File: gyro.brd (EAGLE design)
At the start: 27.9 x 15.2 mm, 12 parts, among them IC3 FXAS21002C

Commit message: gyro gotowe! w lbr pozmieniane poligony
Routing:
- net GND: track 6.35 -> 2.59 mm, vias 14 -> 15
- net MOSI: track 23.6 -> 25.7 mm
- net VDDIO: track 4.77 -> 6.41 mm
- net MISO: track 26.9 -> 27.8 mm

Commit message: gerbery do gyro
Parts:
- renumbered SV1 to SPI, SV2 to ZAS
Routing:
- net GND: vias 15 -> 14
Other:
- board text added: "CLK"
- board text added: "CSA"
- board text added: "CSG"
- board text added: "GND"
- board text added: "INTA"
- board text added: "K. Trzcinski K. Dworakowski 2015"
- board text added: "MISO"
- board text added: "MOSI"
- board text added: "VCC"
- board text added: "X"
- board text added: "Y"

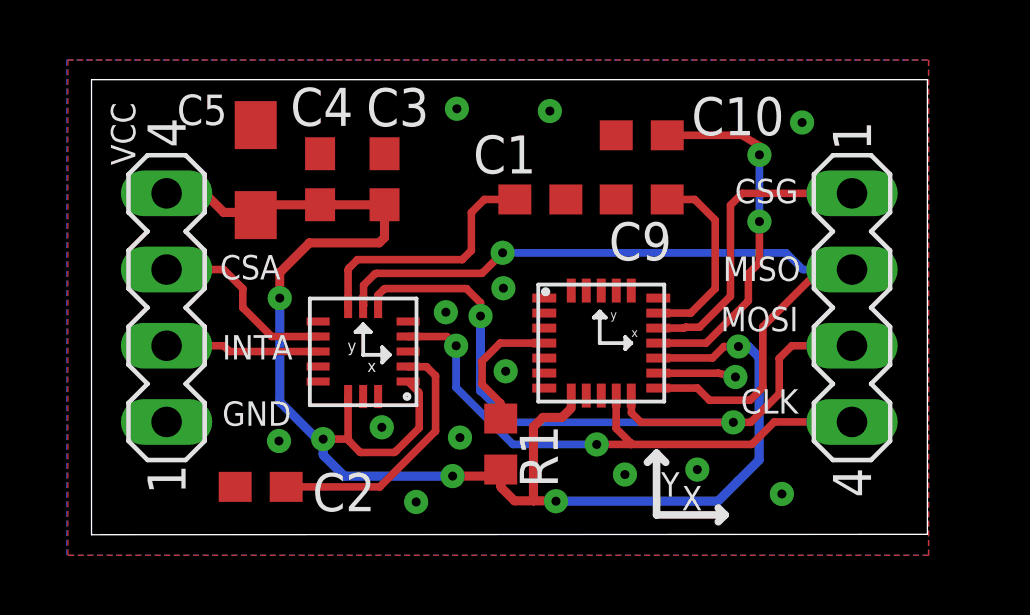
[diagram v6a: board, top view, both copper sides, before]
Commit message: wszystko polaczone, zmiana w gyro z vcc na +3v3
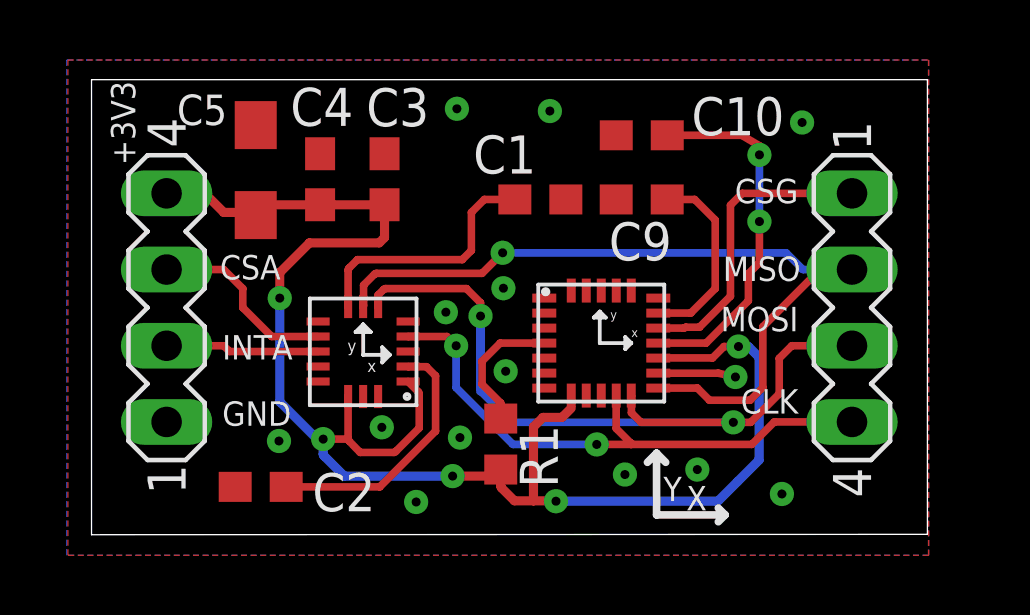
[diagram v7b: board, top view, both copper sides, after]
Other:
- board text added: "+3V3"
- board text removed: "VCC"
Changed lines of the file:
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@@
 <grid distance="3" unitdist="mil" unit="mil" style="lines" multiple="1" display="yes" altdistance="0.5" altunitdist="mil" altunit="mil"/>
 <layers>
-<layer number="1" name="Top" color="4" fill="1" visible="yes" active="yes"/>
+<layer number="1" name="Top" color="4" fill="1" visible="no" active="yes"/>
 <layer number="2" name="Route2" color="1" fill="3" visible="no" active="no"/>
 <layer number="3" name="Route3" color="4" fill="3" visible="no" active="no"/>
@@
 <layer number="14" name="Route14" color="1" fill="6" visible="no" active="no"/>
 <layer number="15" name="Route15" color="4" fill="6" visible="no" active="no"/>
-<layer number="16" name="Bottom" color="1" fill="1" visible="yes" active="yes"/>
+<layer number="16" name="Bottom" color="1" fill="1" visible="no" active="yes"/>
 <layer number="17" name="Pads" color="2" fill="1" visible="yes" active="yes"/>
 <layer number="18" name="Vias" color="2" fill="1" visible="yes" active="yes"/>
 <layer number="19" name="Unrouted" color="6" fill="1" visible="no" active="yes"/>
 <layer number="20" name="Dimension" color="15" fill="1" visible="no" active="yes"/>
-<layer number="21" name="tPlace" color="7" fill="1" visible="yes" active="yes"/>
+<layer number="21" name="tPlace" color="7" fill="1" visible="no" active="yes"/>
 <layer number="22" name="bPlace" color="7" fill="1" visible="yes" active="yes"/>
-<layer number="23" name="tOrigins" color="15" fill="1" visible="yes" active="yes"/>
+<layer number="23" name="tOrigins" color="15" fill="1" visible="no" active="yes"/>
 <layer number="24" name="bOrigins" color="15" fill="1" visible="no" active="yes"/>
-<layer number="25" name="tNames" color="7" fill="1" visible="yes" active="yes"/>
+<layer number="25" name="tNames" color="7" fill="1" visible="no" active="yes"/>
 <layer number="26" name="bNames" color="7" fill="1" visible="yes" active="yes"/>
 <layer number="27" name="tValues" color="7" fill="1" visible="no" active="yes"/>
@@
 <layer number="101" name="Patch_Top" color="12" fill="4" visible="no" active="yes"/>
 <layer number="102" name="Vscore" color="7" fill="1" visible="no" active="yes"/>
-<layer number="103" name="tMap" color="7" fill="1" visible="yes" active="yes"/>
+<layer number="103" name="tMap" color="7" fill="1" visible="no" active="yes"/>
 <layer number="104" name="Name" color="16" fill="1" visible="no" active="yes"/>
 <layer number="105" name="tPlate" color="7" fill="1" visible="no" active="yes"/>
@@
 <text x="26.1366" y="91.8972" size="0.8128" layer="25" rot="R180">CLK</text>
 <text x="6.9342" y="90.678" size="0.8128" layer="25">GND</text>
-<text x="4.0386" y="99.3648" size="0.8128" layer="25" rot="R90">VCC</text>
+<text x="4.0386" y="99.3648" size="0.8128" layer="25" rot="R90">+3V3</text>
 <text x="24.2316" y="94.4118" size="1.4224" layer="26" font="vector" ratio="12" distance="41" rot="MR0">K. Trzcinski
 K. Dworakowski
@@
 <wire x1="23.6982" y1="87.7062" x2="23.4696" y2="87.9348" width="0.254" layer="21"/>
 <wire x1="23.6982" y1="87.7062" x2="23.4696" y2="87.4776" width="0.254" layer="21"/>
-<text x="21.5646" y="88.3158" size="0.8128" layer="21">Y</text>
-<text x="22.2504" y="87.8586" size="0.8128" layer="21">X</text>
+<text x="21.6408" y="88.1634" size="0.8128" layer="21">Y</text>
+<text x="22.4028" y="87.8586" size="0.8128" layer="21">X</text>
 </plain>
 <attributes>

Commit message: poprawa bledow, dodanie rezystorow na wyjsciach stm-glownie w modolach, poprawa elementu 9axis z biblioteki
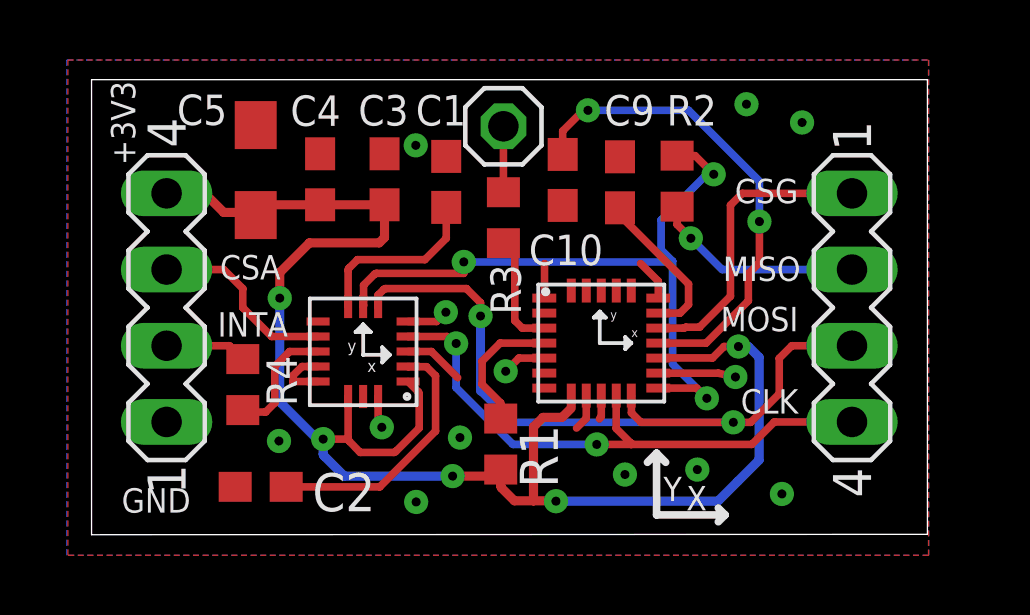
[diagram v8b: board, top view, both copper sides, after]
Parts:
- added INT_G: (no value), pinhead:1X01
- added R2, R3, R4: (no value), rcl:R0603
- moved C1 3.19 mm to (14.4, 98.8), turned to 90 degrees
- moved C10 3.03 mm to (18.3, 98.9), turned to 270 degrees
- moved C9 0.92 mm to (20.2, 98.8), turned to 270 degrees
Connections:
- removed net INT_G: IC3.INT1
- new net N$1: R2.1, SPI.2
- new net N$2: INT_G.1, R3.2
- new net N$3: IC3.INT1, R3.1
- new net N$4: R4.2, ZAS.2
- net INT_A: now also R4.1; no longer ZAS.2
- net MISO: now also R2.2; no longer SPI.2
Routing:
- net GND: track 2.59 -> 15.1 mm, vias 14 -> 13
- net N$1: track 0.00 -> 7.05 mm, vias 0 -> 1
- net N$26: track 12.1 -> 16.3 mm
- net MISO: track 27.8 -> 23.8 mm, vias 1 -> 3
- net N$3: track 0.00 -> 3.82 mm
- net N$4: track 0.00 -> 2.72 mm
- net N$6: track 8.51 -> 5.97 mm
- net N$2: track 0.00 -> 2.20 mm
- net VDDIO: track 6.41 -> 5.30 mm
- net INT_A: track 5.13 -> 4.09 mm
